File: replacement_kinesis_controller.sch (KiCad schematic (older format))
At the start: 39 parts

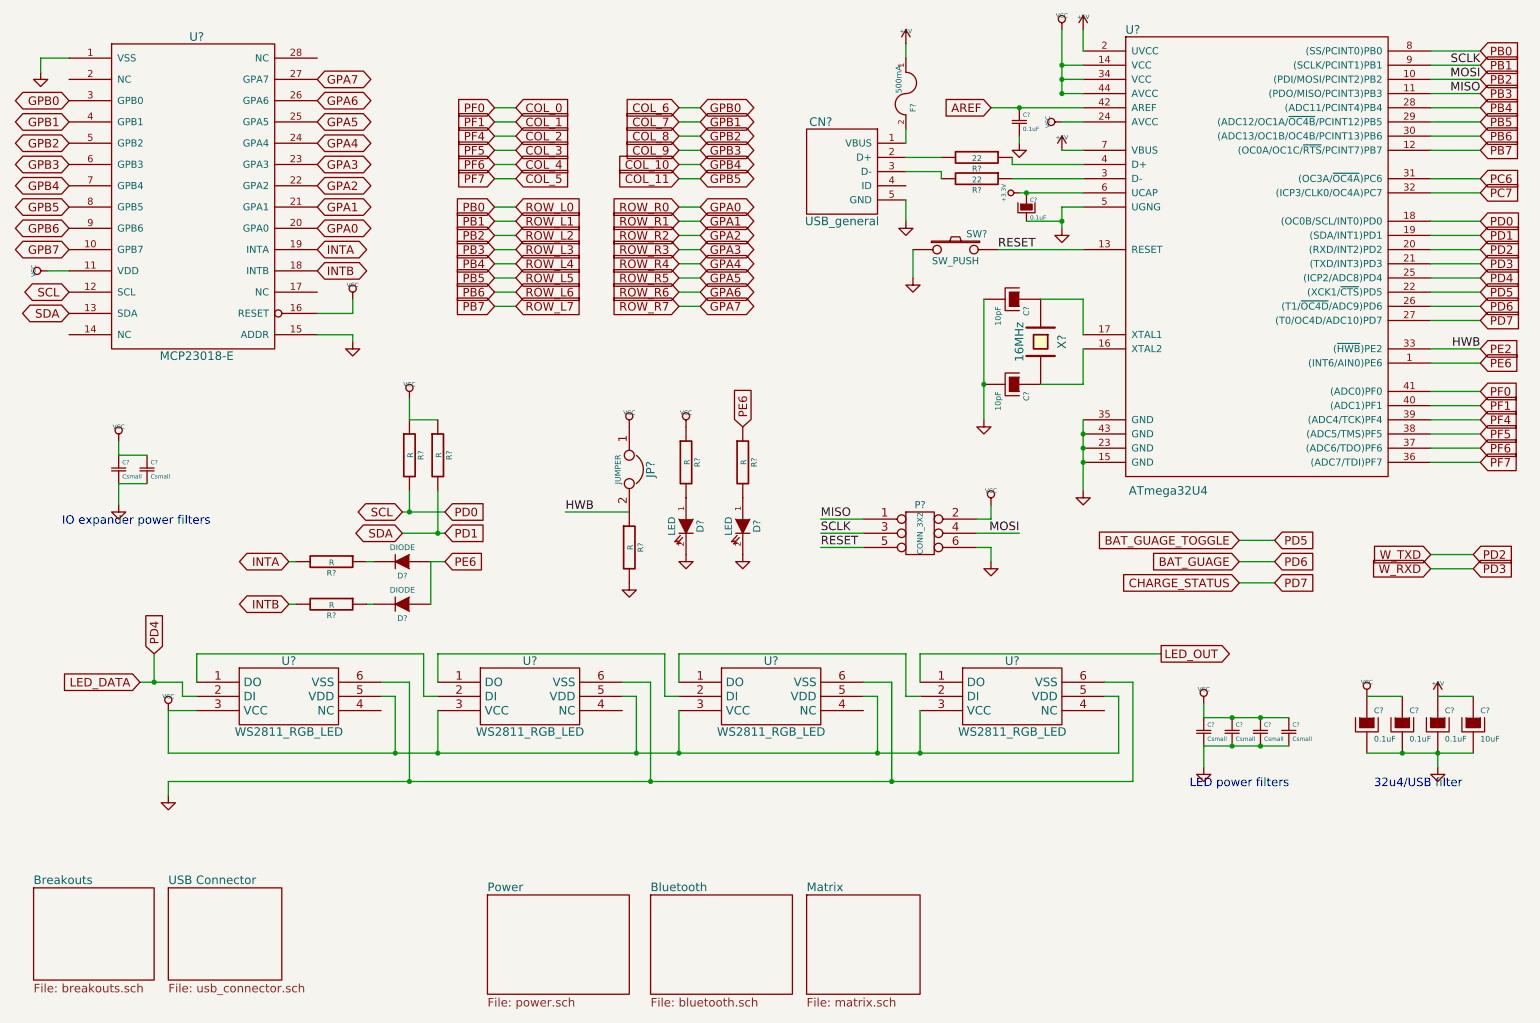
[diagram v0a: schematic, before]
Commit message: Add annotations to parts
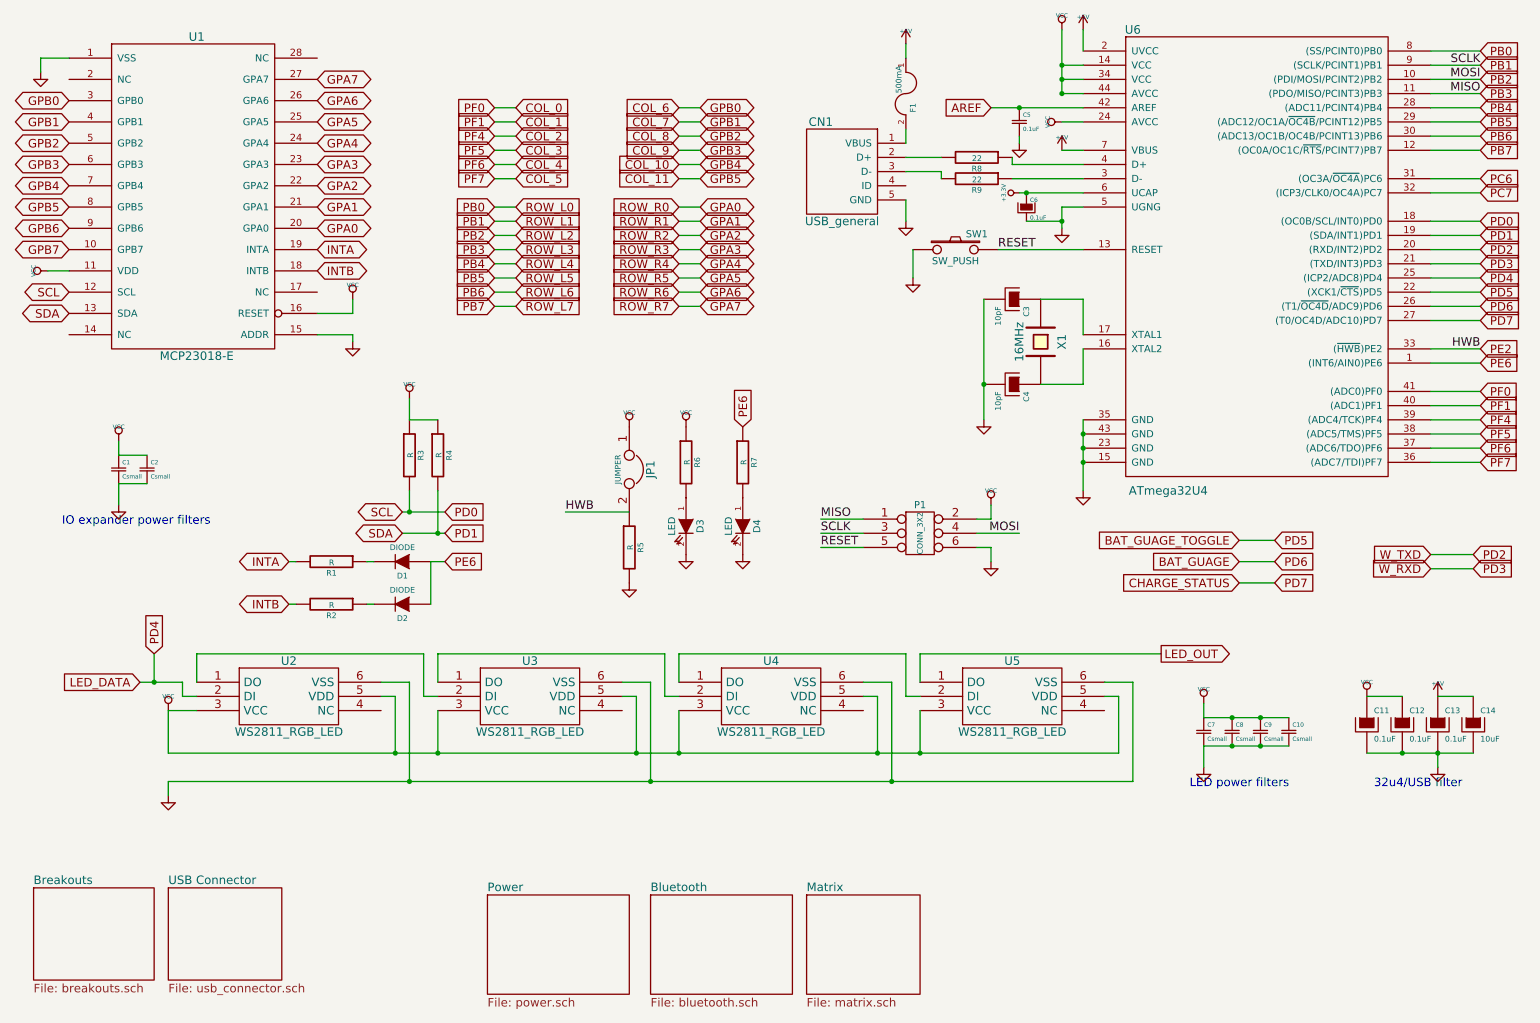
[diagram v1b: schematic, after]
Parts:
- C1, C10, C11, C12, C13, C14, C2, C3, C4, C5, C6, C7, C8, C9: renamed from C?; footprint (none) -> Capacitors_SMD:C_0805_HandSoldering
- CN1: renamed from CN?; footprint (none) -> replacement_kinesis_controller:Pin_Header_Staggered_Straight_1x05
- JP1: renamed from JP?; footprint (none) -> replacement_kinesis_controller:JUMPER_2
- P1: renamed from P?; footprint (none) -> replacement_kinesis_controller:Pin_Header_Staggered_Straight_2x03
- R1, R2, R3, R4, R5, R6, R7, R8, R9: renamed from R?; footprint (none) -> Resistors_SMD:R_0805_HandSoldering
- U1: renamed from U?; footprint (none) -> SMD_Packages:SOIC-28
- gave numbers to parts that had none: 12

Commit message: WT12 breakout headers are now in place
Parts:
- U2, U3, U4, U5: footprint (none) -> replacement_kinesis_controller:LED_RGB_WS2811
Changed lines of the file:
@@
 F 0 "U2" H 2450 5800 60  0000 C CNN
 F 1 "WS2811_RGB_LED" H 2450 5300 60  0000 C CNN
-F 2 "" H 2500 5550 60  0001 C CNN
+F 2 "replacement_kinesis_controller:LED_RGB_WS2811" H 2500 5550 60  0001 C CNN
 F 3 "" H 2500 5550 60  0000 C CNN
 	1    2450 5550
@@
 F 0 "U3" H 4150 5800 60  0000 C CNN
 F 1 "WS2811_RGB_LED" H 4150 5300 60  0000 C CNN
-F 2 "" H 4200 5550 60  0001 C CNN
+F 2 "replacement_kinesis_controller:LED_RGB_WS2811" H 4200 5550 60  0001 C CNN
 F 3 "" H 4200 5550 60  0000 C CNN
 	1    4150 5550
@@
 F 0 "U4" H 5850 5800 60  0000 C CNN
 F 1 "WS2811_RGB_LED" H 5850 5300 60  0000 C CNN
-F 2 "" H 5900 5550 60  0001 C CNN
+F 2 "replacement_kinesis_controller:LED_RGB_WS2811" H 5900 5550 60  0001 C CNN
 F 3 "" H 5900 5550 60  0000 C CNN
 	1    5850 5550
@@
 F 0 "U5" H 7550 5800 60  0000 C CNN
 F 1 "WS2811_RGB_LED" H 7550 5300 60  0000 C CNN
-F 2 "" H 7600 5550 60  0001 C CNN
+F 2 "replacement_kinesis_controller:LED_RGB_WS2811" H 7600 5550 60  0001 C CNN
 F 3 "" H 7600 5550 60  0000 C CNN
 	1    7550 5550

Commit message: Add footprints to regular diodes
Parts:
- D1, D2: footprint (none) -> replacement_kinesis_controller:SOD-323_Handsolder
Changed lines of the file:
@@
 F 0 "D1" H 3250 4700 40  0000 C CNN
 F 1 "DIODE" H 3250 4500 40  0000 C CNN
-F 2 "" H 3250 4600 60  0001 C CNN
+F 2 "replacement_kinesis_controller:SOD-323_Handsolder" H 3250 4600 60  0001 C CNN
 F 3 "" H 3250 4600 60  0000 C CNN
 	1    3250 4600
@@
 F 0 "D2" H 3250 5000 40  0000 C CNN
 F 1 "DIODE" H 3250 4800 40  0000 C CNN
-F 2 "" H 3250 4900 60  0001 C CNN
+F 2 "replacement_kinesis_controller:SOD-323_Handsolder" H 3250 4900 60  0001 C CNN
 F 3 "" H 3250 4900 60  0000 C CNN
 	1    3250 4900

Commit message: Add regular LED footprints
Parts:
- D3, D4: footprint (none) -> LEDs:LED-0805
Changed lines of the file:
@@
 F 0 "D3" H 5250 4450 50  0000 C CNN
 F 1 "LED" H 5250 4250 50  0000 C CNN
-F 2 "" H 5250 4350 60  0001 C CNN
+F 2 "LEDs:LED-0805" H 5250 4350 60  0001 C CNN
 F 3 "" H 5250 4350 60  0000 C CNN
 	1    5250 4350
@@
 F 0 "D4" H 5650 4450 50  0000 C CNN
 F 1 "LED" H 5650 4250 50  0000 C CNN
-F 2 "" H 5650 4350 60  0001 C CNN
+F 2 "LEDs:LED-0805" H 5650 4350 60  0001 C CNN
 F 3 "" H 5650 4350 60  0000 C CNN
 	1    5650 4350

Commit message: Add more footprint mappings
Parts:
- F1: footprint (none) -> Resistors_SMD:R_0805_HandSoldering
- U6: footprint (none) -> Housings_QFP:TQFP-44_10x10mm_Pitch0.8mm
- X1: footprint (none) -> Crystals:Crystal_HC49-SD_SMD
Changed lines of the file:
@@
 F 0 "U6" H 8400 4250 60  0000 C CNN
 F 1 "ATmega32U4" H 8650 1000 60  0000 C CNN
-F 2 "" H 10500 3650 60  0001 C CNN
+F 2 "Housings_QFP:TQFP-44_10x10mm_Pitch0.8mm" H 10500 3650 60  0001 C CNN
 F 3 "" H 10500 3650 60  0000 C CNN
 	1    9300 2550
@@
 F 0 "X1" H 7750 3200 60  0000 C CNN
 F 1 "16MHz" H 7750 2900 60  0000 C CNN
-F 2 "" H 7750 3050 60  0001 C CNN
+F 2 "Crystals:Crystal_HC49-SD_SMD" H 7750 3050 60  0001 C CNN
 F 3 "" H 7750 3050 60  0000 C CNN
 	1    7750 3050
@@
 F 0 "F1" H 6900 1350 40  0000 C CNN
 F 1 "500mA" H 6700 1250 40  0000 C CNN
-F 2 "" H 6800 1300 60  0001 C CNN
+F 2 "Resistors_SMD:R_0805_HandSoldering" H 6800 1300 60  0001 C CNN
 F 3 "" H 6800 1300 60  0000 C CNN
 	1    6800 1300

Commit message: Basically done footprint assignment now...?
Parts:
- SW1: footprint (none) -> Buttons_Switches_SMD:SW_SPST_PTS645
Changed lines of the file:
@@
 F 0 "SW1" H 7300 2510 50  0000 C CNN
 F 1 "SW_PUSH" H 7150 2320 50  0000 C CNN
-F 2 "" H 7150 2400 60  0001 C CNN
+F 2 "Buttons_Switches_SMD:SW_SPST_PTS645" H 7150 2400 60  0001 C CNN
 F 3 "" H 7150 2400 60  0000 C CNN
 	1    7150 2400

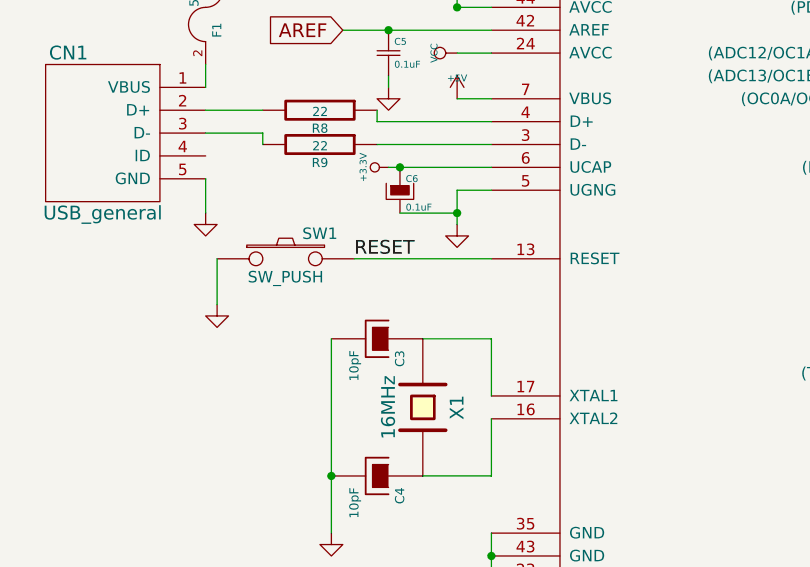
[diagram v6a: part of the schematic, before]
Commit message: A bunch of footprint arranging
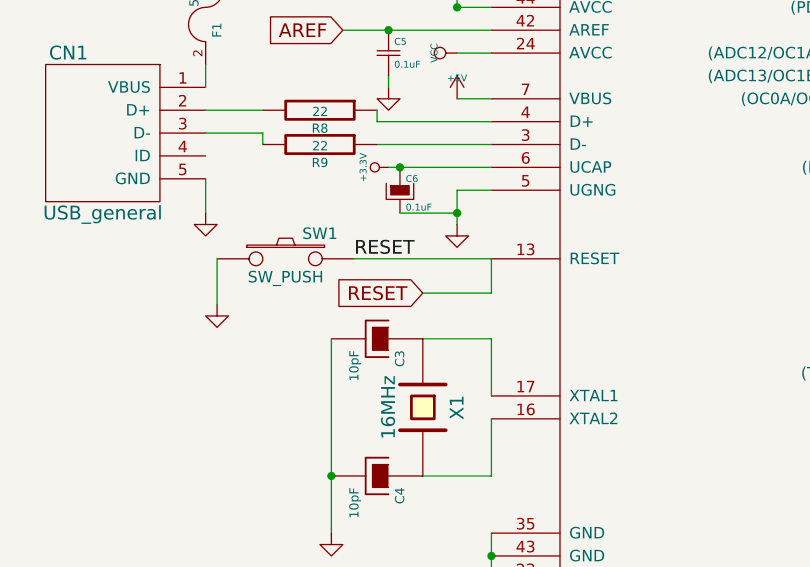
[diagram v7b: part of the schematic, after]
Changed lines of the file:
@@
 $EndComp
 $Comp
-L GND #PWR18
+L GND #PWR01
 U 1 1 54712BE2
 P 7350 3600
-F 0 "#PWR18" H 7350 3600 30  0001 C CNN
+F 0 "#PWR01" H 7350 3600 30  0001 C CNN
 F 1 "GND" H 7350 3530 30  0001 C CNN
 F 2 "" H 7350 3600 60  0000 C CNN
@@
 $EndComp
 $Comp
-L GND #PWR28
+L GND #PWR02
 U 1 1 54712D7E
 P 8050 4100
-F 0 "#PWR28" H 8050 4100 30  0001 C CNN
+F 0 "#PWR02" H 8050 4100 30  0001 C CNN
 F 1 "GND" H 8050 4030 30  0001 C CNN
 F 2 "" H 8050 4100 60  0000 C CNN
@@
 $EndComp
 $Comp
-L +5V #PWR27
+L +5V #PWR03
 U 1 1 54713488
 P 8050 850
-F 0 "#PWR27" H 8050 940 20  0001 C CNN
+F 0 "#PWR03" H 8050 940 20  0001 C CNN
 F 1 "+5V" H 8050 940 30  0000 C CNN
 F 2 "" H 8050 850 60  0000 C CNN
@@
 $EndComp
 $Comp
-L VCC #PWR23
+L VCC #PWR04
 U 1 1 5471349C
 P 7900 850
-F 0 "#PWR23" H 7900 950 30  0001 C CNN
+F 0 "#PWR04" H 7900 950 30  0001 C CNN
 F 1 "VCC" H 7900 950 30  0000 C CNN
 F 2 "" H 7900 850 60  0000 C CNN
@@
 $EndComp
 $Comp
-L GND #PWR26
+L GND #PWR05
 U 1 1 54714355
 P 7900 2250
-F 0 "#PWR26" H 7900 2250 30  0001 C CNN
+F 0 "#PWR05" H 7900 2250 30  0001 C CNN
 F 1 "GND" H 7900 2180 30  0001 C CNN
 F 2 "" H 7900 2250 60  0000 C CNN
@@
 RESET
 $Comp
-L +5V #PWR25
+L +5V #PWR06
 U 1 1 54715465
 P 7900 1700
-F 0 "#PWR25" H 7900 1790 20  0001 C CNN
+F 0 "#PWR06" H 7900 1790 20  0001 C CNN
 F 1 "+5V" H 7900 1790 30  0000 C CNN
 F 2 "" H 7900 1700 60  0000 C CNN
@@
 $EndComp
 $Comp
-L VCC #PWR24
+L VCC #PWR07
 U 1 1 5471554B
 P 7900 1500
-F 0 "#PWR24" H 7900 1600 30  0001 C CNN
+F 0 "#PWR07" H 7900 1600 30  0001 C CNN
 F 1 "VCC" H 7900 1600 30  0000 C CNN
 F 2 "" H 7900 1500 60  0000 C CNN
@@
 RESET
 $Comp
-L VCC #PWR19
+L VCC #PWR08
 U 1 1 5471750B
 P 7400 4200
-F 0 "#PWR19" H 7400 4300 30  0001 C CNN
+F 0 "#PWR08" H 7400 4300 30  0001 C CNN
 F 1 "VCC" H 7400 4300 30  0000 C CNN
 F 2 "" H 7400 4200 60  0000 C CNN
@@
 $EndComp
 $Comp
-L GND #PWR20
+L GND #PWR09
 U 1 1 5471751D
 P 7400 4600
-F 0 "#PWR20" H 7400 4600 30  0001 C CNN
+F 0 "#PWR09" H 7400 4600 30  0001 C CNN
 F 1 "GND" H 7400 4530 30  0001 C CNN
 F 2 "" H 7400 4600 60  0000 C CNN
@@
 $EndComp
 $Comp
-L GND #PWR17
+L GND #PWR010
 U 1 1 54718A7A
 P 6850 2600
-F 0 "#PWR17" H 6850 2600 30  0001 C CNN
+F 0 "#PWR010" H 6850 2600 30  0001 C CNN
 F 1 "GND" H 6850 2530 30  0001 C CNN
 F 2 "" H 6850 2600 60  0000 C CNN
@@
 $EndComp
 $Comp
-L GND #PWR16
+L GND #PWR011
 U 1 1 547192FE
 P 6800 2200
-F 0 "#PWR16" H 6800 2200 30  0001 C CNN
+F 0 "#PWR011" H 6800 2200 30  0001 C CNN
 F 1 "GND" H 6800 2130 30  0001 C CNN
 F 2 "" H 6800 2200 60  0000 C CNN
@@
 $EndComp
 $Comp
-L +5V #PWR15
+L +5V #PWR012
 U 1 1 547195A0
 P 6800 950
-F 0 "#PWR15" H 6800 1040 20  0001 C CNN
+F 0 "#PWR012" H 6800 1040 20  0001 C CNN
 F 1 "+5V" H 6800 1040 30  0000 C CNN
 F 2 "" H 6800 950 60  0000 C CNN
@@
 $EndComp
 $Comp
-L +3.3V #PWR22
+L +3.3V #PWR013
 U 1 1 5471A4EC
 P 7600 2000
-F 0 "#PWR22" H 7600 1960 30  0001 C CNN
+F 0 "#PWR013" H 7600 1960 30  0001 C CNN
 F 1 "+3.3V" H 7600 2110 30  0000 C CNN
 F 2 "" H 7600 2000 60  0000 C CNN
@@
 $EndComp
 $Comp
-L VCC #PWR31
+L VCC #PWR014
 U 1 1 547237FE
 P 10050 5550
-F 0 "#PWR31" H 10050 5650 30  0001 C CNN
+F 0 "#PWR014" H 10050 5650 30  0001 C CNN
 F 1 "VCC" H 10050 5650 30  0000 C CNN
 F 2 "" H 10050 5550 60  0000 C CNN
@@
 $EndComp
 $Comp
-L +5V #PWR32
+L +5V #PWR015
 U 1 1 54723804
 P 10550 5550
-F 0 "#PWR32" H 10550 5640 20  0001 C CNN
+F 0 "#PWR015" H 10550 5640 20  0001 C CNN
 F 1 "+5V" H 10550 5640 30  0000 C CNN
 F 2 "" H 10550 5550 60  0000 C CNN
@@
 $EndComp
 $Comp
-L GND #PWR33
+L GND #PWR016
 U 1 1 5472380A
 P 10550 6050
-F 0 "#PWR33" H 10550 6050 30  0001 C CNN
+F 0 "#PWR016" H 10550 6050 30  0001 C CNN
 F 1 "GND" H 10550 5980 30  0001 C CNN
 F 2 "" H 10550 6050 60  0000 C CNN
@@
 $EndComp
 $Comp
-L VCC #PWR12
+L VCC #PWR017
 U 1 1 54C9D8DB
 P 5250 3650
-F 0 "#PWR12" H 5250 3750 30  0001 C CNN
+F 0 "#PWR017" H 5250 3750 30  0001 C CNN
 F 1 "VCC" H 5250 3750 30  0000 C CNN
 F 2 "" H 5250 3650 60  0000 C CNN
@@
 $EndComp
 $Comp
-L VCC #PWR10
+L VCC #PWR018
 U 1 1 54C9D977
 P 4850 3650
-F 0 "#PWR10" H 4850 3750 30  0001 C CNN
+F 0 "#PWR018" H 4850 3750 30  0001 C CNN
 F 1 "VCC" H 4850 3750 30  0000 C CNN
 F 2 "" H 4850 3650 60  0000 C CNN
@@
 $EndComp
 $Comp
-L GND #PWR13
+L GND #PWR019
 U 1 1 54C9D99F
 P 5250 4550
-F 0 "#PWR13" H 5250 4550 30  0001 C CNN
+F 0 "#PWR019" H 5250 4550 30  0001 C CNN
 F 1 "GND" H 5250 4480 30  0001 C CNN
 F 2 "" H 5250 4550 60  0000 C CNN
@@
 $EndComp
 $Comp
-L GND #PWR11
+L GND #PWR020
 U 1 1 54C9D9C7
 P 4850 4750
-F 0 "#PWR11" H 4850 4750 30  0001 C CNN
+F 0 "#PWR020" H 4850 4750 30  0001 C CNN
 F 1 "GND" H 4850 4680 30  0001 C CNN
 F 2 "" H 4850 4750 60  0000 C CNN
@@
 $EndComp
 $Comp
-L GND #PWR14
+L GND #PWR021
 U 1 1 54C9D9EF
 P 5650 4550
-F 0 "#PWR14" H 5650 4550 30  0001 C CNN
+F 0 "#PWR021" H 5650 4550 30  0001 C CNN
 F 1 "GND" H 5650 4480 30  0001 C CNN
 F 2 "" H 5650 4550 60  0000 C CNN
@@
 GPB7
 $Comp
-L GND #PWR1
+L GND #PWR022
 U 1 1 54CB370B
 P 700 1150
-F 0 "#PWR1" H 700 1150 30  0001 C CNN
+F 0 "#PWR022" H 700 1150 30  0001 C CNN
 F 1 "GND" H 700 1080 30  0001 C CNN
 F 2 "" H 700 1150 60  0000 C CNN
@@
 $EndComp
 $Comp
-L VCC #PWR2
+L VCC #PWR023
 U 1 1 54CB597A
 P 750 2550
-F 0 "#PWR2" H 750 2650 30  0001 C CNN
+F 0 "#PWR023" H 750 2650 30  0001 C CNN
 F 1 "VCC" H 750 2650 30  0000 C CNN
 F 2 "" H 750 2550 60  0000 C CNN
@@
 $EndComp
 $Comp
-L GND #PWR8
+L GND #PWR024
 U 1 1 54CB76C3
 P 2900 3050
-F 0 "#PWR8" H 2900 3050 30  0001 C CNN
+F 0 "#PWR024" H 2900 3050 30  0001 C CNN
 F 1 "GND" H 2900 2980 30  0001 C CNN
 F 2 "" H 2900 3050 60  0000 C CNN
@@
 $EndComp
 $Comp
-L VCC #PWR7
+L VCC #PWR025
 U 1 1 54CB7764
 P 2900 2750
-F 0 "#PWR7" H 2900 2850 30  0001 C CNN
+F 0 "#PWR025" H 2900 2850 30  0001 C CNN
 F 1 "VCC" H 2900 2850 30  0000 C CNN
 F 2 "" H 2900 2750 60  0000 C CNN
@@
 $EndComp
 $Comp
-L VCC #PWR5
+L VCC #PWR026
 U 1 1 54D46834
 P 1600 5650
-F 0 "#PWR5" H 1600 5750 30  0001 C CNN
+F 0 "#PWR026" H 1600 5750 30  0001 C CNN
 F 1 "VCC" H 1600 5750 30  0000 C CNN
 F 2 "" H 1600 5650 60  0000 C CNN
@@
 $EndComp
 $Comp
-L GND #PWR6
+L GND #PWR027
 U 1 1 54D4A2BE
 P 1600 6250
-F 0 "#PWR6" H 1600 6250 30  0001 C CNN
+F 0 "#PWR027" H 1600 6250 30  0001 C CNN
 F 1 "GND" H 1600 6180 30  0001 C CNN
 F 2 "" H 1600 6250 60  0000 C CNN
@@
 $EndComp
 $Comp
-L VCC #PWR9
+L VCC #PWR028
 U 1 1 54DD6701
 P 3300 3450
-F 0 "#PWR9" H 3300 3550 30  0001 C CNN
+F 0 "#PWR028" H 3300 3550 30  0001 C CNN
 F 1 "VCC" H 3300 3550 30  0000 C CNN
 F 2 "" H 3300 3450 60  0000 C CNN
@@
 Connection ~ 1500 5450
 $Comp
-L VCC #PWR29
+L VCC #PWR029
 U 1 1 54E6DA2C
 P 8900 5600
-F 0 "#PWR29" H 8900 5700 30  0001 C CNN
+F 0 "#PWR029" H 8900 5700 30  0001 C CNN
 F 1 "VCC" H 8900 5700 30  0000 C CNN
 F 2 "" H 8900 5600 60  0000 C CNN
@@
 $EndComp
 $Comp
-L GND #PWR30
+L GND #PWR030
 U 1 1 54E6DBB8
 P 8900 6050
-F 0 "#PWR30" H 8900 6050 30  0001 C CNN
+F 0 "#PWR030" H 8900 6050 30  0001 C CNN
 F 1 "GND" H 8900 5980 30  0001 C CNN
 F 2 "" H 8900 6050 60  0000 C CNN
@@
 $EndSheet
 $Comp
-L VCC #PWR3
+L VCC #PWR031
 U 1 1 54E71458
 P 1250 3750
-F 0 "#PWR3" H 1250 3850 30  0001 C CNN
+F 0 "#PWR031" H 1250 3850 30  0001 C CNN
 F 1 "VCC" H 1250 3850 30  0000 C CNN
 F 2 "" H 1250 3750 60  0000 C CNN
@@
 $EndComp
 $Comp
-L GND #PWR4
+L GND #PWR032
 U 1 1 54E7145E
 P 1250 4200
-F 0 "#PWR4" H 1250 4200 30  0001 C CNN
+F 0 "#PWR032" H 1250 4200 30  0001 C CNN
 F 1 "GND" H 1250 4130 30  0001 C CNN
 F 2 "" H 1250 4200 60  0000 C CNN
@@
 $EndComp
 $Comp
-L GND #PWR21
+L GND #PWR033
 U 1 1 54E8CE58
 P 7600 1650
-F 0 "#PWR21" H 7600 1650 30  0001 C CNN
+F 0 "#PWR033" H 7600 1650 30  0001 C CNN
 F 1 "GND" H 7600 1580 30  0001 C CNN
 F 2 "" H 7600 1650 60  0000 C CNN
@@
 Wire Wire Line
 	10500 4650 10800 4650
+Text GLabel 7750 2550 0    60   Input ~ 0
+RESET
+Wire Wire Line
+	7750 2550 8050 2550
+Wire Wire Line
+	8050 2550 8050 2400
 $EndSCHEMATC
